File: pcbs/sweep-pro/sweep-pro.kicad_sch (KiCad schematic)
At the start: 49 parts, among them SW1 SW_PUSH-kbd, SW10 SW_PUSH-kbd, SW11 SW_PUSH-kbd, SW12 SW_PUSH-kbd, SW13 SW_PUSH-kbd, SW14 SW_PUSH-kbd, SW15 SW_PUSH-kbd, SW16 SW_PUSH-kbd, SW17 SW_PUSH-kbd, SW2 SW_PUSH-kbd, SW3 SW_PUSH-kbd, SW4 SW_PUSH-kbd, SW5 SW_PUSH-kbd, SW6 SW_PUSH-kbd, SW7 SW_PUSH-kbd, SW8 SW_PUSH-kbd, SW9 SW_PUSH-kbd, U1 ProMicro-kbd

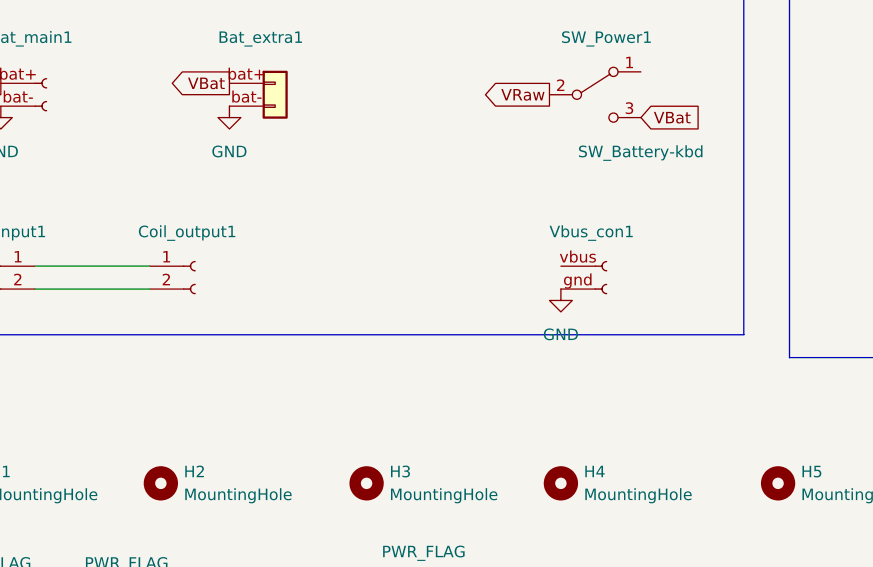
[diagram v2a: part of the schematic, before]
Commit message: add filled area (complete board)
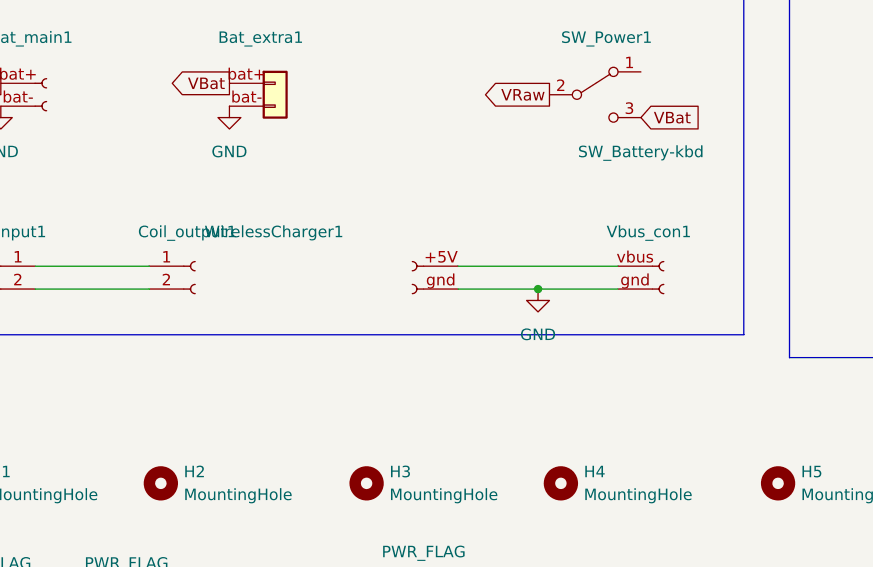
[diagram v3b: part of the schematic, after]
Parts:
- added WirelessCharger1: Conn_01x02_Female, mylib:VBus_pad_reversible, symbol Connector:Conn_01x02_Female
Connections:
- net GND: now also WirelessCharger1.gnd (GND)
- net at Vbus_con1.vbus (Pin_1): now also WirelessCharger1.+5V
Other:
- moved on the sheet: Vbus_con1
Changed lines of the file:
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@@
   (junction (at 163.83 88.9) (diameter 0) (color 0 0 0 0)
   )
+  (junction (at 86.36 154.94) (diameter 0) (color 0 0 0 0)
+  )
   (junction (at 189.23 88.9) (diameter 0) (color 0 0 0 0)
   )
@@
     (stroke (width 0) (type default) (color 0 0 0 0))
   )
+  (wire (pts (xy 77.47 152.4) (xy 95.25 152.4))
+    (stroke (width 0) (type default) (color 0 0 0 0))
+  )
   (wire (pts (xy 240.03 88.9) (xy 260.35 88.9))
     (stroke (width 0) (type default) (color 0 0 0 0))
@@
     (stroke (width 0) (type default) (color 0 0 0 0))
   )
+  (wire (pts (xy 86.36 154.94) (xy 95.25 154.94))
+    (stroke (width 0) (type default) (color 0 0 0 0))
+  )
   (wire (pts (xy 189.23 67.31) (xy 214.63 67.31))
     (stroke (width 0) (type default) (color 0 0 0 0))
@@
   )
   (polyline (pts (xy 114.3 162.56) (xy 276.86 162.56))
+    (stroke (width 0) (type default) (color 0 0 0 0))
+  )
+  (wire (pts (xy 77.47 154.94) (xy 86.36 154.94))
     (stroke (width 0) (type default) (color 0 0 0 0))
   )
@@
     (pin "1")
     (pin "2")
-  )
-  (symbol (lib_id "power:GND") (at 88.9 154.94 0) (unit 1)
-    (in_bom yes) (on_board yes) (fields_autoplaced)
-    (property "Reference" "#PWR0109" (id 0) (at 88.9 161.29 0)
-      (effects (font (size 1.27 1.27)) hide)
-    )
-    (property "Value" "GND" (id 1) (at 88.9 160.02 0))
-    (property "Footprint" "" (id 2) (at 88.9 154.94 0)
-      (effects (font (size 1.27 1.27)) hide)
-    )
-    (property "Datasheet" "" (id 3) (at 88.9 154.94 0)
-      (effects (font (size 1.27 1.27)) hide)
-    )
-    (pin "1")
   )
   (symbol (lib_id "power:GND") (at 26.67 134.62 0) (unit 1)
@@
     (pin "1")
   )
-  (symbol (lib_name "Conn_01x02_Female_1") (lib_id "Connector:Conn_01x02_Female") (at 93.98 152.4 0) (unit 1)
+  (symbol (lib_name "Conn_01x02_Female_1") (lib_id "Connector:Conn_01x02_Female") (at 100.33 152.4 0) (unit 1)
     (in_bom no) (on_board yes)
-    (property "Reference" "Vbus_con1" (id 0) (at 87.63 148.59 0)
+    (property "Reference" "Vbus_con1" (id 0) (at 93.98 148.59 0)
       (effects (font (size 1.27 1.27)) (justify left))
     )
-    (property "Value" "Conn_01x02_Female" (id 1) (at 95.25 154.9399 0)
-      (effects (font (size 1.27 1.27)) (justify left) hide)
-    )
-    (property "Footprint" "mylib:VBus_pad_reversible" (id 2) (at 93.98 158.75 0)
-      (effects (font (size 1.27 1.27)) hide)
-    )
-    (property "Datasheet" "~" (id 3) (at 93.98 152.4 0)
+    (property "Value" "Conn_01x02_Female" (id 1) (at 101.6 154.9399 0)
+      (effects (font (size 1.27 1.27)) (justify left) hide)
+    )
+    (property "Footprint" "mylib:VBus_pad_reversible" (id 2) (at 100.33 158.75 0)
+      (effects (font (size 1.27 1.27)) hide)
+    )
+    (property "Datasheet" "~" (id 3) (at 100.33 152.4 0)
       (effects (font (size 1.27 1.27)) hide)
     )
     (pin "gnd")
     (pin "vbus")
+  )
+  (symbol (lib_id "power:GND") (at 86.36 154.94 0) (unit 1)
+    (in_bom yes) (on_board yes) (fields_autoplaced)
+    (property "Reference" "#PWR?" (id 0) (at 86.36 161.29 0)
+      (effects (font (size 1.27 1.27)) hide)
+    )
+    (property "Value" "GND" (id 1) (at 86.36 160.02 0))
+    (property "Footprint" "" (id 2) (at 86.36 154.94 0)
+      (effects (font (size 1.27 1.27)) hide)
+    )
+    (property "Datasheet" "" (id 3) (at 86.36 154.94 0)
+      (effects (font (size 1.27 1.27)) hide)
+    )
+    (pin "1")
   )
   (symbol (lib_id "power:PWR_FLAG") (at 40.64 190.5 0) (unit 1)
@@
       (effects (font (size 1.27 1.27)) hide)
     )
+  )
+  (symbol (lib_name "Conn_01x02_Female_2") (lib_id "Connector:Conn_01x02_Female") (at 72.39 152.4 0) (mirror y) (unit 1)
+    (in_bom no) (on_board yes)
+    (property "Reference" "WirelessCharger1" (id 0) (at 64.77 148.59 0)
+      (effects (font (size 1.27 1.27)) (justify left))
+    )
+    (property "Value" "Conn_01x02_Female" (id 1) (at 73.66 154.9399 0)
+      (effects (font (size 1.27 1.27)) (justify left) hide)
+    )
+    (property "Footprint" "mylib:VBus_pad_reversible" (id 2) (at 72.39 148.59 0)
+      (effects (font (size 1.27 1.27)) hide)
+    )
+    (property "Datasheet" "~" (id 3) (at 72.39 152.4 0)
+      (effects (font (size 1.27 1.27)) hide)
+    )
+    (pin "+5V")
+    (pin "gnd")
   )
   (symbol (lib_id "Mechanical:MountingHole") (at 44.45 176.53 0) (unit 1)
@@
       (reference "#PWR0108") (unit 1) (value "GND") (footprint "")
     )
-    (path "/1ccaf9c1-07e5-4528-834a-88b5e92cc69d"
-      (reference "#PWR0109") (unit 1) (value "GND") (footprint "")
-    )
     (path "/6dfb8131-ca0e-42be-a304-9ed244979805"
       (reference "#PWR0110") (unit 1) (value "GND") (footprint "")
     )
+    (path "/7ca8d14c-7c7b-4a75-a5d5-a86307f5c64a"
+      (reference "#PWR?") (unit 1) (value "GND") (footprint "")
+    )
     (path "/5a75c756-d045-47cd-91a8-22173b1f50b9"
       (reference "Bat_extra1") (unit 1) (value "Conn_Battery_pluggable") (footprint "mylib:Battery_connector_lim_reversible")
@@
       (reference "Vbus_con1") (unit 1) (value "Conn_01x02_Female") (footprint "mylib:VBus_pad_reversible")
     )
-  )
+    (path "/a096bc0e-4800-429c-8cf2-2103191ee8c0"
+      (reference "WirelessCharger1") (unit 1) (value "Conn_01x02_Female") (footprint "mylib:VBus_pad_reversible")
+    )
+  )

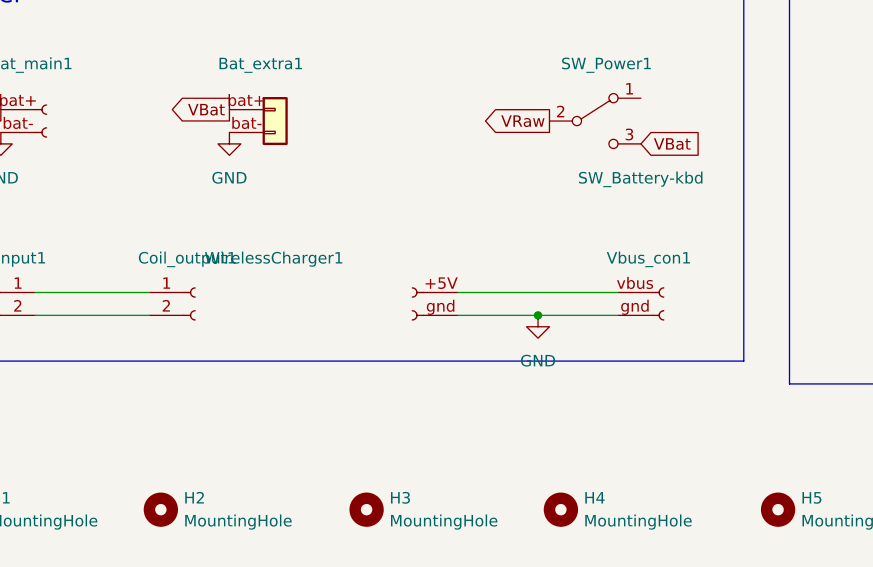
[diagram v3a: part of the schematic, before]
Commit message: change the position of battery connector for better case design. and change the angle of thumb cluster and board outline for better looking.
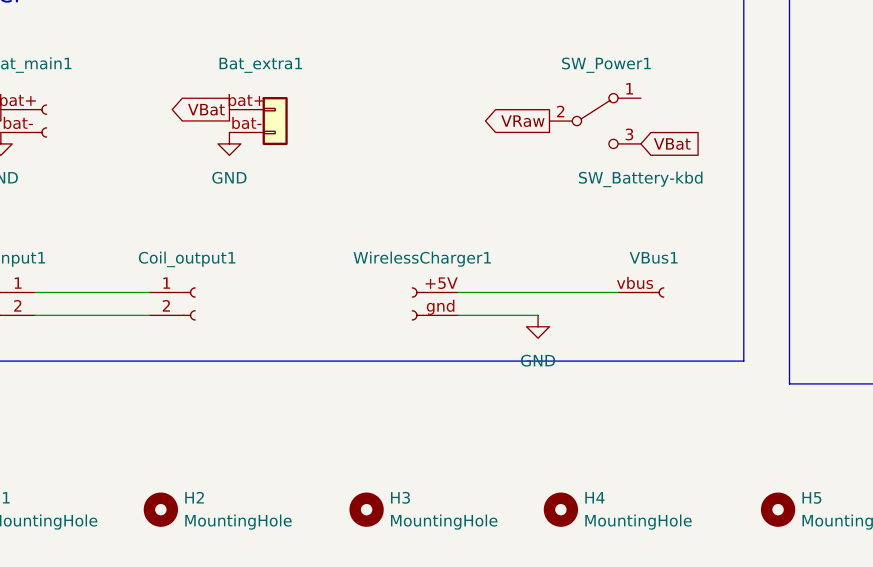
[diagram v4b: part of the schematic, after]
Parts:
- removed Vbus_con1: Conn_01x02_Female, mylib:VBus_pad_reversible, symbol Connector:Conn_01x02_Female
- added VBus1: Conn_01x01_Female, mylib:GND_1pin_conn, symbol Connector:Conn_01x01_Female
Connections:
- net at WirelessCharger1.+5V: now also VBus1.vbus (VBus)
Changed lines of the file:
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@@
   (junction (at 163.83 88.9) (diameter 0) (color 0 0 0 0)
   )
-  (junction (at 86.36 154.94) (diameter 0) (color 0 0 0 0)
-  )
   (junction (at 189.23 88.9) (diameter 0) (color 0 0 0 0)
   )
@@
   )
   (wire (pts (xy 214.63 46.99) (xy 214.63 49.53))
-    (stroke (width 0) (type default) (color 0 0 0 0))
-  )
-  (wire (pts (xy 86.36 154.94) (xy 95.25 154.94))
     (stroke (width 0) (type default) (color 0 0 0 0))
   )
@@
     (pin "1")
   )
-  (symbol (lib_name "Conn_01x02_Female_1") (lib_id "Connector:Conn_01x02_Female") (at 100.33 152.4 0) (unit 1)
-    (in_bom no) (on_board yes)
-    (property "Reference" "Vbus_con1" (id 0) (at 93.98 148.59 0)
-      (effects (font (size 1.27 1.27)) (justify left))
-    )
-    (property "Value" "Conn_01x02_Female" (id 1) (at 101.6 154.9399 0)
-      (effects (font (size 1.27 1.27)) (justify left) hide)
-    )
-    (property "Footprint" "mylib:VBus_pad_reversible" (id 2) (at 100.33 158.75 0)
-      (effects (font (size 1.27 1.27)) hide)
-    )
-    (property "Datasheet" "~" (id 3) (at 100.33 152.4 0)
-      (effects (font (size 1.27 1.27)) hide)
-    )
-    (pin "gnd")
-    (pin "vbus")
-  )
   (symbol (lib_id "power:GND") (at 86.36 154.94 0) (unit 1)
     (in_bom yes) (on_board yes) (fields_autoplaced)
-    (property "Reference" "#PWR?" (id 0) (at 86.36 161.29 0)
+    (property "Reference" "#PWR0109" (id 0) (at 86.36 161.29 0)
       (effects (font (size 1.27 1.27)) hide)
     )
@@
     (pin "1")
     (pin "2")
+  )
+  (symbol (lib_id "Connector:Conn_01x01_Female") (at 100.33 152.4 0) (unit 1)
+    (in_bom no) (on_board yes)
+    (property "Reference" "VBus1" (id 0) (at 96.52 148.59 0)
+      (effects (font (size 1.27 1.27)) (justify left))
+    )
+    (property "Value" "Conn_01x01_Female" (id 1) (at 101.6 153.6699 0)
+      (effects (font (size 1.27 1.27)) (justify left) hide)
+    )
+    (property "Footprint" "mylib:GND_1pin_conn" (id 2) (at 100.33 157.48 0)
+      (effects (font (size 1.27 1.27)) hide)
+    )
+    (property "Datasheet" "~" (id 3) (at 100.33 152.4 0)
+      (effects (font (size 1.27 1.27)) hide)
+    )
+    (pin "vbus")
   )
   (symbol (lib_id "Mechanical:MountingHole") (at 88.9 176.53 0) (unit 1)
@@
   (symbol (lib_name "Conn_01x02_Female_2") (lib_id "Connector:Conn_01x02_Female") (at 72.39 152.4 0) (mirror y) (unit 1)
     (in_bom no) (on_board yes)
-    (property "Reference" "WirelessCharger1" (id 0) (at 64.77 148.59 0)
+    (property "Reference" "WirelessCharger1" (id 0) (at 81.28 148.59 0)
       (effects (font (size 1.27 1.27)) (justify left))
     )
@@
       (reference "#PWR0108") (unit 1) (value "GND") (footprint "")
     )
+    (path "/7ca8d14c-7c7b-4a75-a5d5-a86307f5c64a"
+      (reference "#PWR0109") (unit 1) (value "GND") (footprint "")
+    )
     (path "/6dfb8131-ca0e-42be-a304-9ed244979805"
       (reference "#PWR0110") (unit 1) (value "GND") (footprint "")
     )
-    (path "/7ca8d14c-7c7b-4a75-a5d5-a86307f5c64a"
-      (reference "#PWR?") (unit 1) (value "GND") (footprint "")
-    )
     (path "/5a75c756-d045-47cd-91a8-22173b1f50b9"
       (reference "Bat_extra1") (unit 1) (value "Conn_Battery_pluggable") (footprint "mylib:Battery_connector_lim_reversible")
@@
       (reference "U1") (unit 1) (value "ProMicro-kbd") (footprint "mylib:ProMicro_Jumpers")
     )
-    (path "/73dd947b-966d-4493-99fa-7050d7c1fe3b"
-      (reference "Vbus_con1") (unit 1) (value "Conn_01x02_Female") (footprint "mylib:VBus_pad_reversible")
+    (path "/818c4b18-5450-4c45-b440-7a14d20c3048"
+      (reference "VBus1") (unit 1) (value "Conn_01x01_Female") (footprint "mylib:GND_1pin_conn")
     )
     (path "/a096bc0e-4800-429c-8cf2-2103191ee8c0"

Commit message: change mouting hole diameter to 3.2mm
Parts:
- H5: footprint MountingHole:MountingHole_2.2mm_M2_ISO7380_Pad_TopBottom -> MountingHole:MountingHole_3.2mm_M3_DIN965
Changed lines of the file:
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@@
       (effects (font (size 1.27 1.27)) (justify left))
     )
-    (property "Footprint" "MountingHole:MountingHole_2.2mm_M2_ISO7380_Pad_TopBottom" (id 2) (at 113.03 176.53 0)
+    (property "Footprint" "MountingHole:MountingHole_3.2mm_M3_DIN965" (id 2) (at 113.03 176.53 0)
       (effects (font (size 1.27 1.27)) hide)
     )
@@
     )
     (path "/9dd58876-f968-4cd0-b2ad-422f53c41329"
-      (reference "H5") (unit 1) (value "MountingHole") (footprint "MountingHole:MountingHole_2.2mm_M2_ISO7380_Pad_TopBottom")
+      (reference "H5") (unit 1) (value "MountingHole") (footprint "MountingHole:MountingHole_3.2mm_M3_DIN965")
     )
     (path "/05029a69-fbde-4ca1-b8ce-fe1db7482fff"
